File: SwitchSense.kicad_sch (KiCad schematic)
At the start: 7 parts, among them J10 Molex 43045-0400, Q3 AO3400A

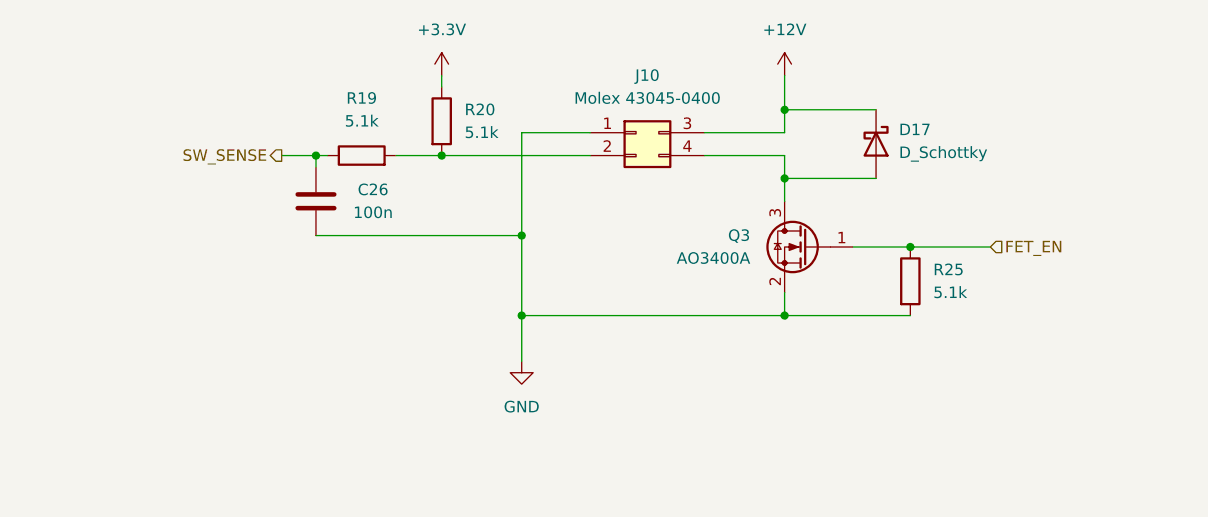
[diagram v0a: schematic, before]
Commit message: updated pinout, begin layout
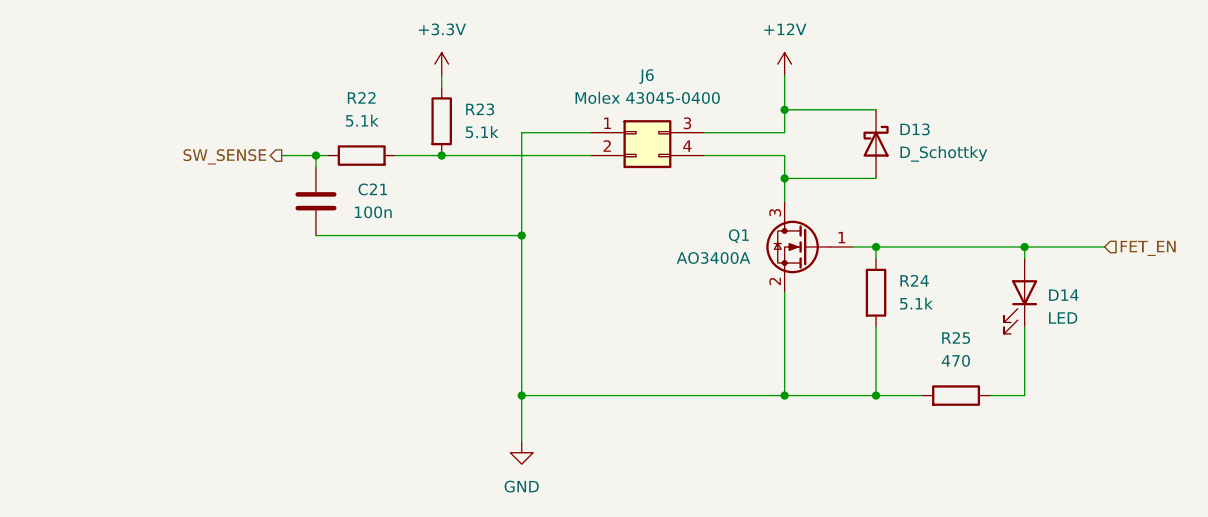
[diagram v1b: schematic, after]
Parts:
- added D14: LED, LED_SMD:LED_0603_1608Metric_Pad1.05x0.95mm_HandSolder, symbol Device:LED
- added R25: 470, Resistor_SMD:R_0603_1608Metric_Pad0.98x0.95mm_HandSolder, symbol Device:R
- renumbered C26 to C21, D17 to D13, J10 to J6, Q3 to Q1, R19 to R22, R20 to R23, R25 to R24
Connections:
- net FET_EN: now also D14.2 (A)
- net GND: now also R25.2
- new net: D14.1 (K), R25.1
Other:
- moved on the sheet: R24

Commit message: dual H/V compatible Molex footprints, corrected STM32 pinout
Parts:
- J6: footprint Connector_Molex:Molex_Micro-Fit_3.0_43045-0400_2x02_P3.00mm_Horizontal -> Project_Library:Molex_Micro-Fit_3.0_43045-0400_2x02_P3.00mm_Horizontal_VerticalCompatible
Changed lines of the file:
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@@
 			)
 		)
-		(property "Footprint" "Connector_Molex:Molex_Micro-Fit_3.0_43045-0400_2x02_P3.00mm_Horizontal"
+		(property "Footprint" "Project_Library:Molex_Micro-Fit_3.0_43045-0400_2x02_P3.00mm_Horizontal_VerticalCompatible"
 			(at 137.16 60.96 0)
 			(hide yes)

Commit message: add zener diodes to inputs
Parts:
- added D33: D_Zener, Diode_SMD:D_SOD-323_HandSoldering, symbol Device:D_Zener
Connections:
- net GND: now also D33.2 (A)
- net SW_SENSE: now also D33.1 (K)
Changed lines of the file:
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@@
 	(paper "A4")
 	(junction
+		(at 101.6 72.39)
+		(diameter 0)
+		(color 0 0 0 0)
+	)
+	(junction
+		(at 101.6 63.5)
+		(diameter 0)
+		(color 0 0 0 0)
+	)
+	(junction
 		(at 153.67 66.04)
 		(diameter 0)
@@
 	)
 	(junction
-		(at 101.6 63.5)
+		(at 86.36 63.5)
 		(diameter 0)
 		(color 0 0 0 0)
@@
 	(wire
 		(pts
+			(xy 86.36 63.5) (xy 101.6 63.5)
+		)
+		(stroke
+			(width 0)
+			(type default)
+		)
+	)
+	(wire
+		(pts
+			(xy 86.36 72.39) (xy 101.6 72.39)
+		)
+		(stroke
+			(width 0)
+			(type default)
+		)
+	)
+	(wire
+		(pts
 			(xy 153.67 66.04) (xy 163.83 66.04)
 		)
@@
 	(wire
 		(pts
-			(xy 97.79 63.5) (xy 101.6 63.5)
+			(xy 81.28 63.5) (xy 86.36 63.5)
 		)
 		(stroke
@@
 		(pts
 			(xy 144.78 63.5) (xy 153.67 63.5)
+		)
+		(stroke
+			(width 0)
+			(type default)
+		)
+	)
+	(wire
+		(pts
+			(xy 86.36 64.77) (xy 86.36 63.5)
 		)
 		(stroke
@@
 	(hierarchical_label "SW_SENSE"
 		(shape output)
-		(at 97.79 63.5 180)
+		(at 81.28 63.5 180)
 		(effects
 			(font
@@
 		)
 	)
+	(symbol
+		(lib_id "Device:D_Zener")
+		(at 86.36 68.58 270)
+		(unit 1)
+		(body_style 1)
+		(exclude_from_sim no)
+		(in_bom yes)
+		(on_board yes)
+		(in_pos_files yes)
+		(dnp no)
+		(fields_autoplaced yes)
+		(property "Reference" "D33"
+			(at 88.9 67.3099 90)
+			(show_name no)
+			(do_not_autoplace no)
+			(effects
+				(font
+					(size 1.27 1.27)
+				)
+				(justify left)
+			)
+		)
+		(property "Value" "D_Zener"
+			(at 88.9 69.8499 90)
+			(show_name no)
+			(do_not_autoplace no)
+			(effects
+				(font
+					(size 1.27 1.27)
+				)
+				(justify left)
+			)
+		)
+		(property "Footprint" "Diode_SMD:D_SOD-323_HandSoldering"
+			(at 86.36 68.58 0)
+			(hide yes)
+			(show_name no)
+			(do_not_autoplace no)
+			(effects
+				(font
+					(size 1.27 1.27)
+				)
+			)
+		)
+		(property "Datasheet" ""
+			(at 86.36 68.58 0)
+			(hide yes)
+			(show_name no)
+			(do_not_autoplace no)
+			(effects
+				(font
+					(size 1.27 1.27)
+				)
+			)
+		)
+		(property "Description" "Zener diode"
+			(at 86.36 68.58 0)
+			(hide yes)
+			(show_name no)
+			(do_not_autoplace no)
+			(effects
+				(font
+					(size 1.27 1.27)
+				)
+			)
+		)
+		(pin "1"
+		)
+		(pin "2"
+		)
+		(instances
+			(project "RSC-LV3-SwitchSense"
+				(path "/ea09e839-df61-4c3f-abdc-aa7ae2f772fe/f5995ec4-65d7-405d-8186-52c2665d3026/19ff984b-2558-4eca-abbf-d6f3f8114e5c"
+					(reference "D36")
+					(unit 1)
+				)
+				(path "/ea09e839-df61-4c3f-abdc-aa7ae2f772fe/f5995ec4-65d7-405d-8186-52c2665d3026/284bac0b-8034-4fc0-8bac-ddd1b681bd4f"
+					(reference "D41")
+					(unit 1)
+				)
+				(path "/ea09e839-df61-4c3f-abdc-aa7ae2f772fe/f5995ec4-65d7-405d-8186-52c2665d3026/28e395e2-6c16-4ec7-acf6-7618cc9764d3"
+					(reference "D38")
+					(unit 1)
+				)
+				(path "/ea09e839-df61-4c3f-abdc-aa7ae2f772fe/f5995ec4-65d7-405d-8186-52c2665d3026/49e2602c-0e28-48e3-8de9-60f653caff1e"
+					(reference "D39")
+					(unit 1)
+				)
+				(path "/ea09e839-df61-4c3f-abdc-aa7ae2f772fe/f5995ec4-65d7-405d-8186-52c2665d3026/534a184d-974f-41ce-8992-ae1f57bd74dc"
+					(reference "D42")
+					(unit 1)
+				)
+				(path "/ea09e839-df61-4c3f-abdc-aa7ae2f772fe/f5995ec4-65d7-405d-8186-52c2665d3026/862166ed-b51d-4620-ba31-eee105b454d0"
+					(reference "D37")
+					(unit 1)
+				)
+				(path "/ea09e839-df61-4c3f-abdc-aa7ae2f772fe/f5995ec4-65d7-405d-8186-52c2665d3026/9c5262a1-60c4-4352-a39a-e500a05938ea"
+					(reference "D35")
+					(unit 1)
+				)
+				(path "/ea09e839-df61-4c3f-abdc-aa7ae2f772fe/f5995ec4-65d7-405d-8186-52c2665d3026/af8ad5bd-9f8e-4586-b290-343a1e36b522"
+					(reference "D33")
+					(unit 1)
+				)
+				(path "/ea09e839-df61-4c3f-abdc-aa7ae2f772fe/f5995ec4-65d7-405d-8186-52c2665d3026/c97204d1-d3bf-45a2-8b98-28e8b0acd966"
+					(reference "D40")
+					(unit 1)
+				)
+				(path "/ea09e839-df61-4c3f-abdc-aa7ae2f772fe/f5995ec4-65d7-405d-8186-52c2665d3026/fcbb757c-2a69-4639-a8d3-b03126b0d3c2"
+					(reference "D34")
+					(unit 1)
+				)
+			)
+		)
+	)
